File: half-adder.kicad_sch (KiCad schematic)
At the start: 69 parts, among them J1 A, J2 B, J3 C, J4 OUTPUT, J5 CARRY OUT, J6 5V, J7 GROUND, Q13 NPN, Q15 NPN, Q2 NPN, Q20 NPN, Q24 NPN, Q7 NPN

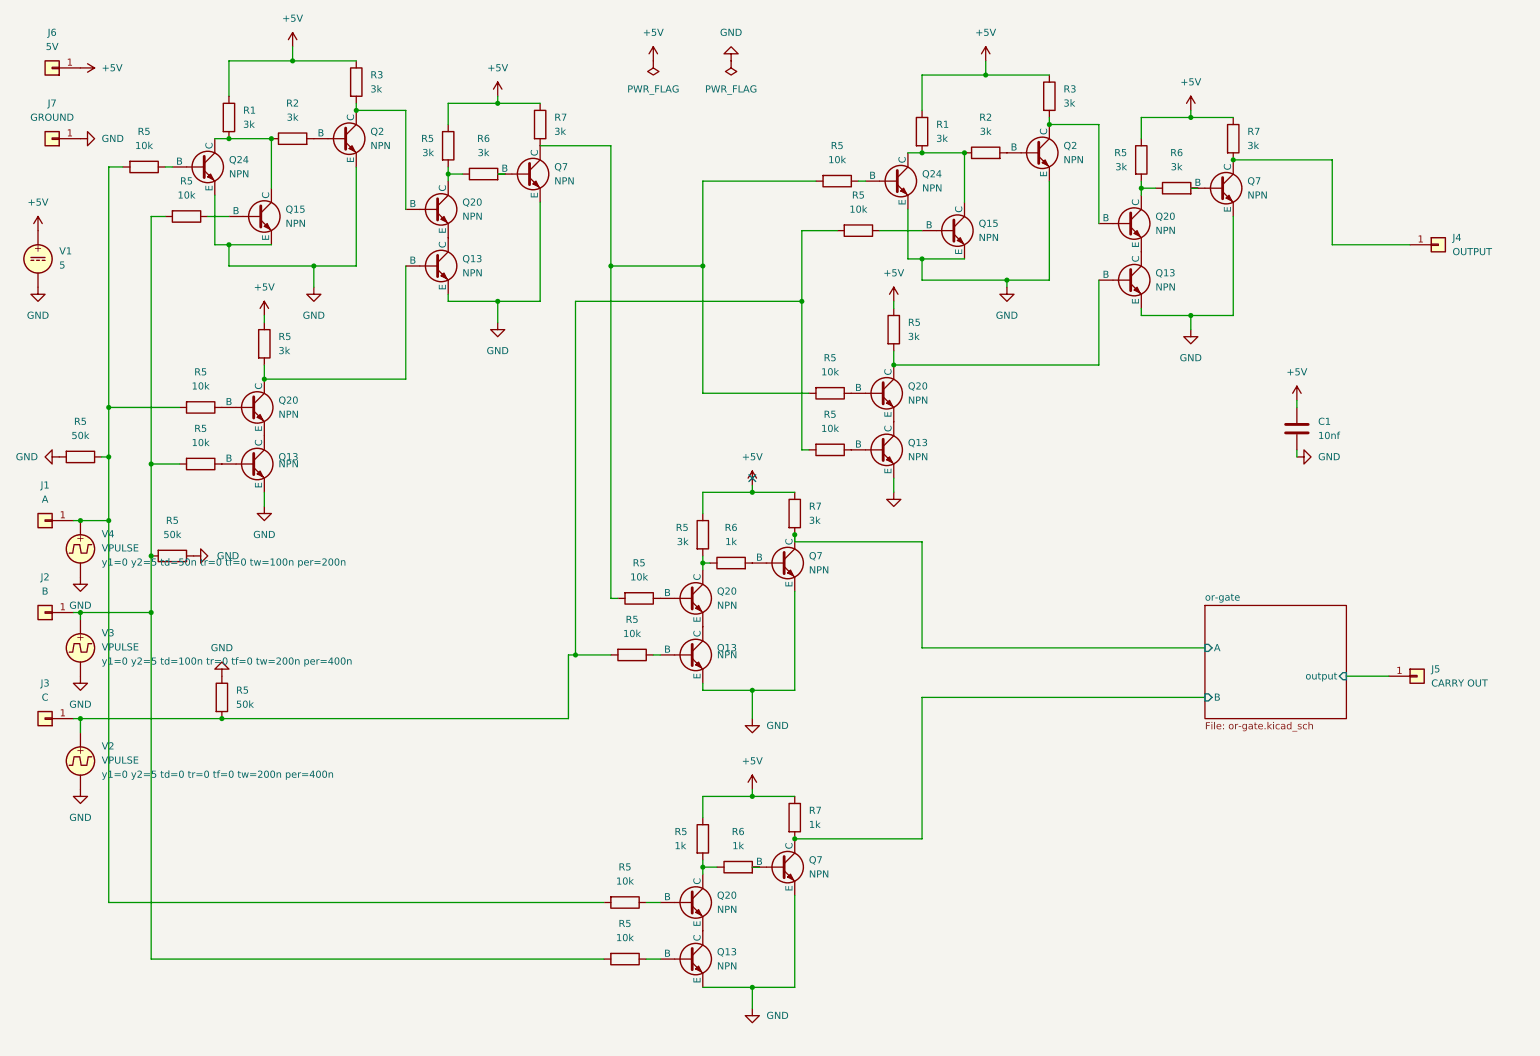
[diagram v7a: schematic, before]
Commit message: replaced circuitry in half adder with reusable gates
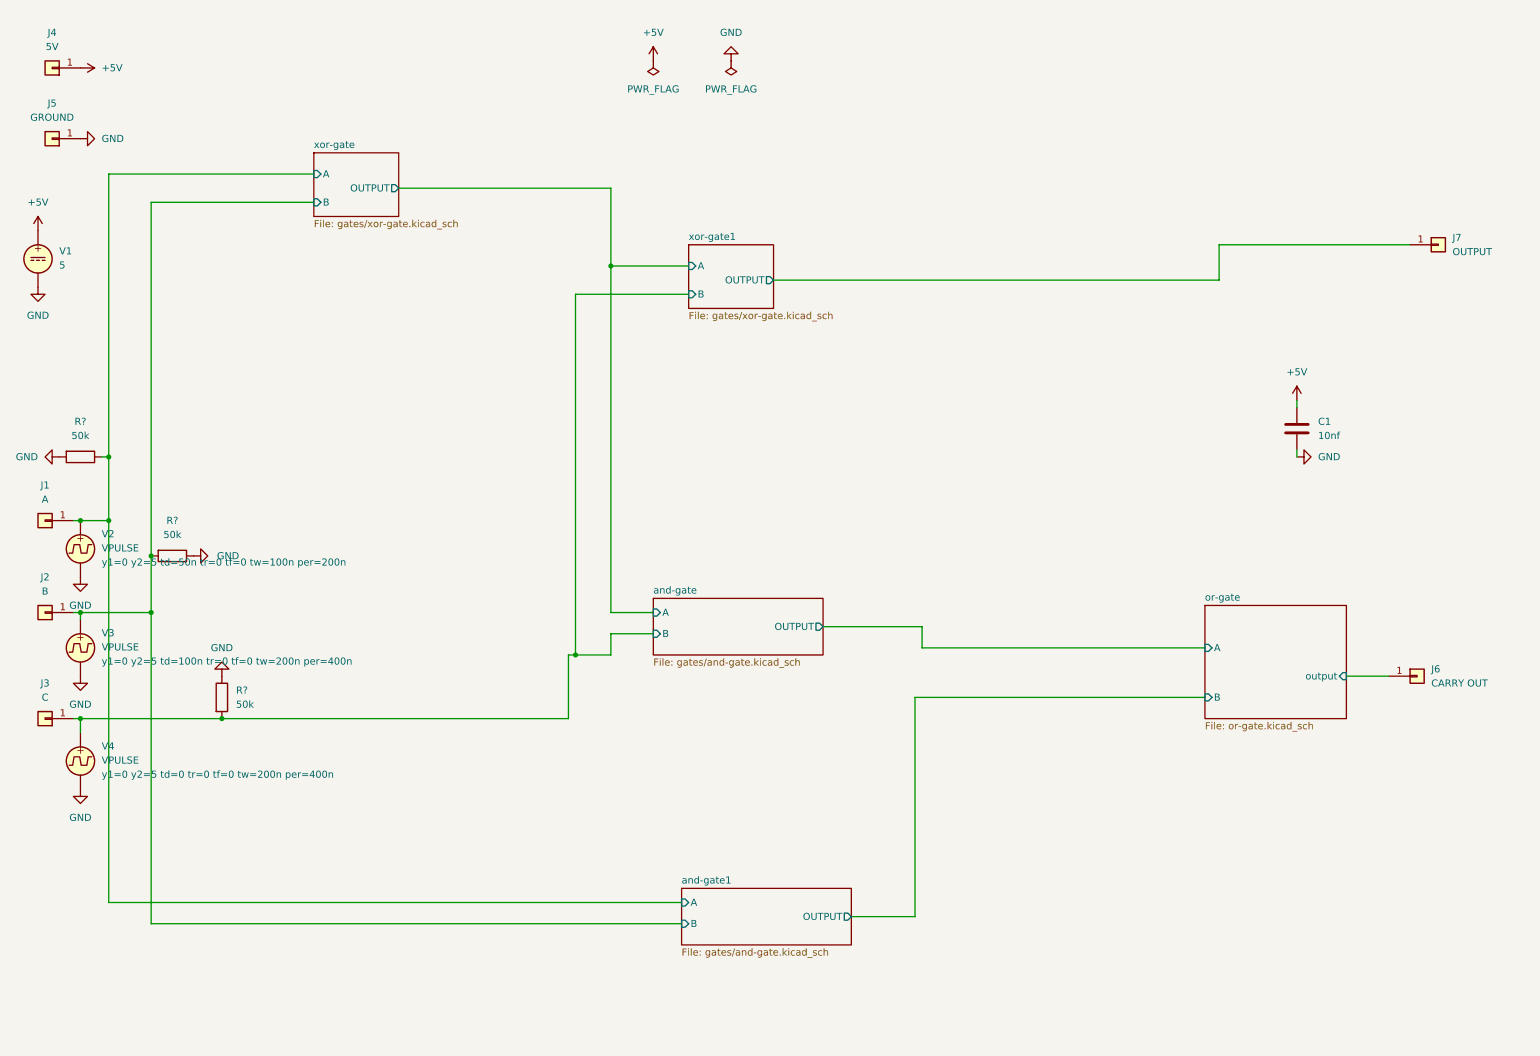
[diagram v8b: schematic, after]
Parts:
- removed Q13 (x6), Q15 (x2), Q2 (x2), Q20 (x6), Q24 (x2), Q7 (x4): NPN, SOT-23-3_L2.9-W1.6-P1.90-LS2.8-BR:SOT-23-3_L2.9-W1.6-P1.90-LS2.8-BR, symbol Simulation_SPICE:NPN
- removed R1 (x2), R2 (x2), R3 (x2), R5 (x5), R6 (x2), R7 (x3): 3k, R0603:R0603, symbol Device:R
- removed R5 (x12): 10k, R0603:R0603, symbol Device:R
- removed R5, R6 (x2), R7: 1k, R0603:R0603, symbol Device:R
- renumbered J6 to J4, J7 to J5, J5 to J6, J4 to J7, R5 to R?, V4 to V2, V2 to V4
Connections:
- net and-gate/B: now reaches J3.1 (Pin_1), R?.2, V4.1
- net xor-gate1/OUTPUT: now reaches J7.1 (Pin_1)
- net and-gate1/B: now reaches J2.1 (Pin_1), R?.2, V3.1
- net and-gate1/A: now reaches J1.1 (Pin_1), R?.1, V2.1
- no-connect marks 1 -> 0
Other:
- added sheet and-gate (gates/and-gate.kicad_sch)
- added sheet and-gate1 (gates/and-gate.kicad_sch)
- added sheet xor-gate (gates/xor-gate.kicad_sch)
- added sheet xor-gate1 (gates/xor-gate.kicad_sch)
